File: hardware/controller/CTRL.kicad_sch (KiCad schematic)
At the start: 0 parts

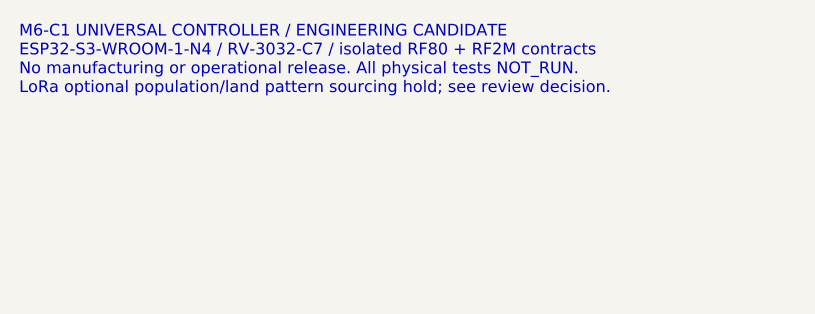
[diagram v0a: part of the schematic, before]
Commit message: M6-C1R1: protect pack identity input and review USB ESD topology
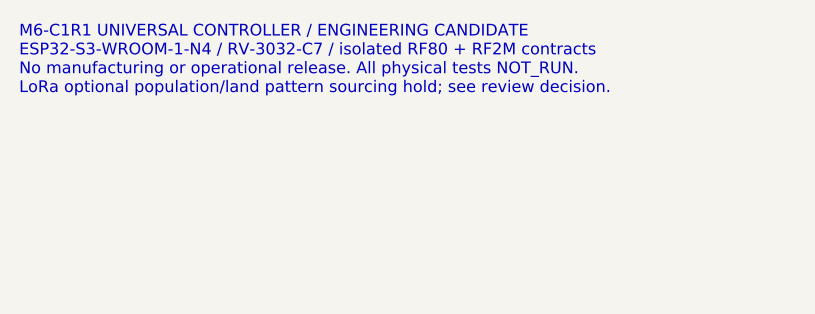
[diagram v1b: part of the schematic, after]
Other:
- note added: "M6-C1R1 UNIVERSAL CONTROLLER / ENGINEERING CANDIDATE ESP32-S3-WROOM-1-N4 / RV-3032-C7 / isolated RF80 + RF2M contracts No manufacturing or operational release. All physical tests NOT_RUN. LoRa optional population/land pattern sourcing hold; see review decision."
- note removed: "M6-C1 UNIVERSAL CONTROLLER / ENGINEERING CANDIDATE ESP32-S3-WROOM-1-N4 / RV-3032-C7 / isolated RF80 + RF2M contracts No manufacturing or operational release. All physical tests NOT_RUN. LoRa optional population/land pattern sourcing hold; see review decision."

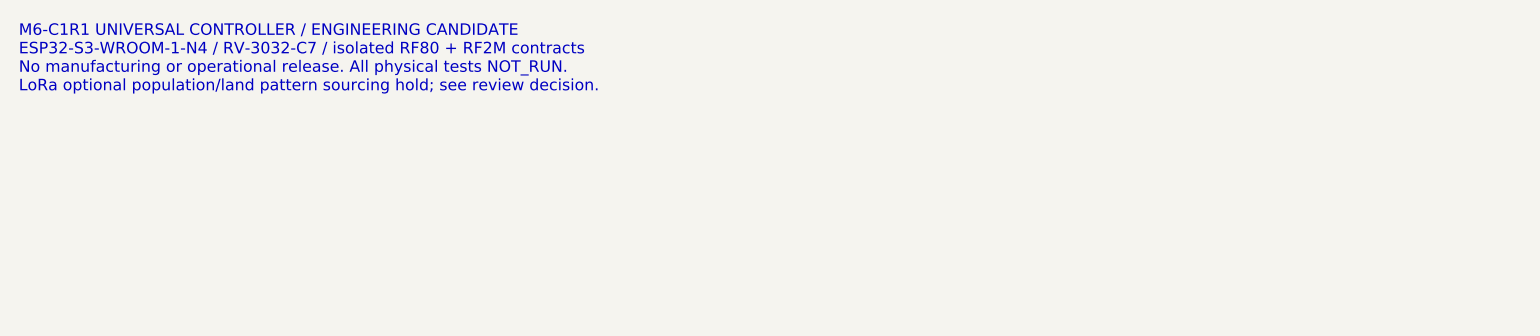
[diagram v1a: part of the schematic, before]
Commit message: M6-L1: close dual-band Silicontra footprint and RF feed review
Verify TR4/TR8 supplier aliases and all 22 nominal module terminals; retain
the common RF signal feed and Hirose lands. Remove a local ground-fill
intrusion in the full U.FL underbody keep-out and correct the module body
outline and unused DIO3 label.

Add explicit no-radio/433/868 assembly records, fail-disabled band/policy
fixtures, native-geometry mutations, tolerance RF calculations and fresh
standard-JLCPCB fabrication/assembly exports with source-bound manifests.

KiCad 10.0.6 ERC/DRC warnings/errors, unrouted and parity all zero. Preserve
704 pad assertions, 36 RF pins, 4096 enable cases, R1 protection/DFM tests,
46 host tests and strict C11 fixture. Physical qualification NOT_RUN.
Independent manufacturing review candidate only; no acceptance tag.
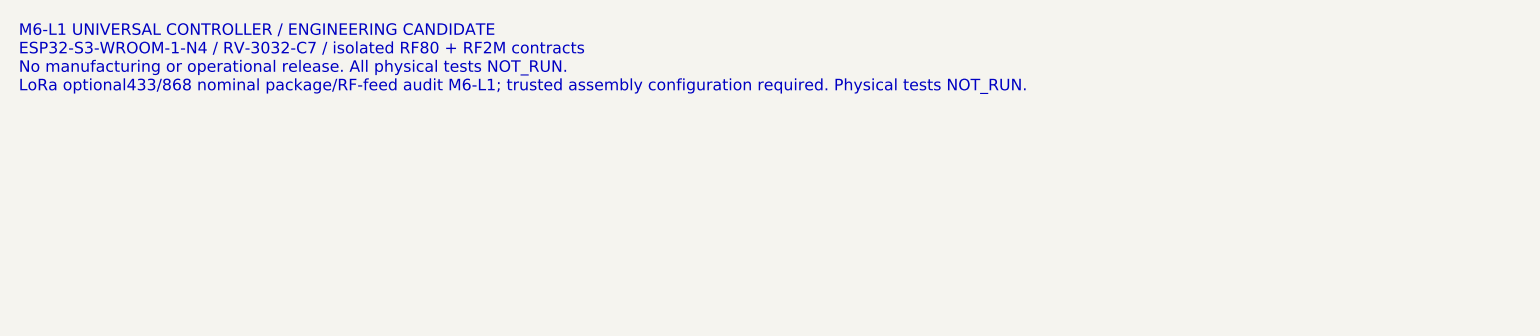
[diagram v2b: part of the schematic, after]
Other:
- note added: "M6-L1 UNIVERSAL CONTROLLER / ENGINEERING CANDIDATE ESP32-S3-WROOM-1-N4 / RV-3032-C7 / isolated RF80 + RF2M contracts No manufacturing or operational release. All physical tests NOT_RUN. LoRa optional433/868 nominal package/RF-feed audit M6-L1; trusted assembly configuration required. Physical tests NOT_RUN."
- note removed: "M6-C1R1 UNIVERSAL CONTROLLER / ENGINEERING CANDIDATE ESP32-S3-WROOM-1-N4 / RV-3032-C7 / isolated RF80 + RF2M contracts No manufacturing or operational release. All physical tests NOT_RUN. LoRa optional population/land pattern sourcing hold; see review decision."

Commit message: M6-L2 — External antenna, FoxPro2 interface and GPIO expansion
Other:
- added sheet 11 FoxPro / 1 (11_FoxPro.kicad_sch)
- added sheet 11 FoxPro / 2 (11_FoxPro_2.kicad_sch)
- added sheet 12 GPIO expansion / 1 (12_GPIO_expansion.kicad_sch)
- added sheet 13 service straps / 1 (13_service_straps.kicad_sch)
